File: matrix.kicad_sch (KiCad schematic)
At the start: 134 parts, among them SW1 ESC`, SW10 #9, SW11 #0, SW12 -_, SW13 =+, SW14 BACKSPACE, SW15 DELETE, SW16 TAB, SW17 Q, SW18 W, SW19 E, SW2 #1, SW20 R, SW21 T, SW22 Y, SW23 U, SW24 I, SW25 O, SW26 P, SW27 [{, SW28 }], SW29 \|, SW3 #2, SW30 PAGEDN, SW31 CAPSLOCK, SW32 A, SW33 S, SW34 D, SW35 F, SW36 G, SW37 H, SW38 J, SW39 K, SW4 #3, SW40 L, SW41 ;:, SW42 '", SW43 ENTER, SW44 INSERT, SW45 SHIFT, SW46 Z, SW47 X, SW48 C, SW49 V, SW5 #4, SW50 B, SW51 N, SW52 M, SW53 ,<, SW54 .>, SW55 /?, SW56 CAPSLOCK, SW57 UP, SW58 SHIFT, SW59 CTRL, SW6 #5, SW60 ALT, SW61 COMMAND, SW62 SPACE, SW63 ALT, SW64 `~, SW65 LEFT, SW66 DOWN, SW67 RIGHT, SW7 #6, SW8 #7, SW9 #8

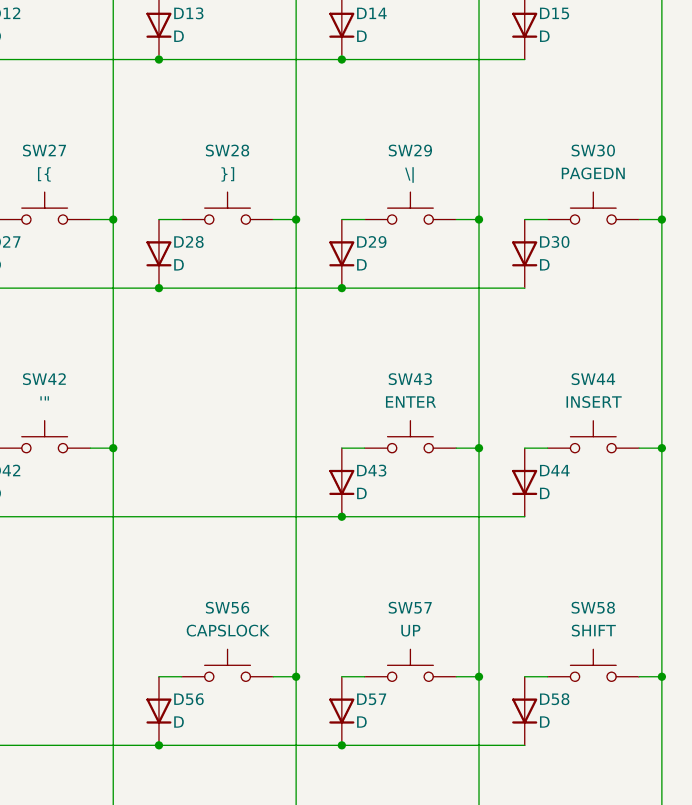
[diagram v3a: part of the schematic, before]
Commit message: PCB Started
need to properly locate pcb components
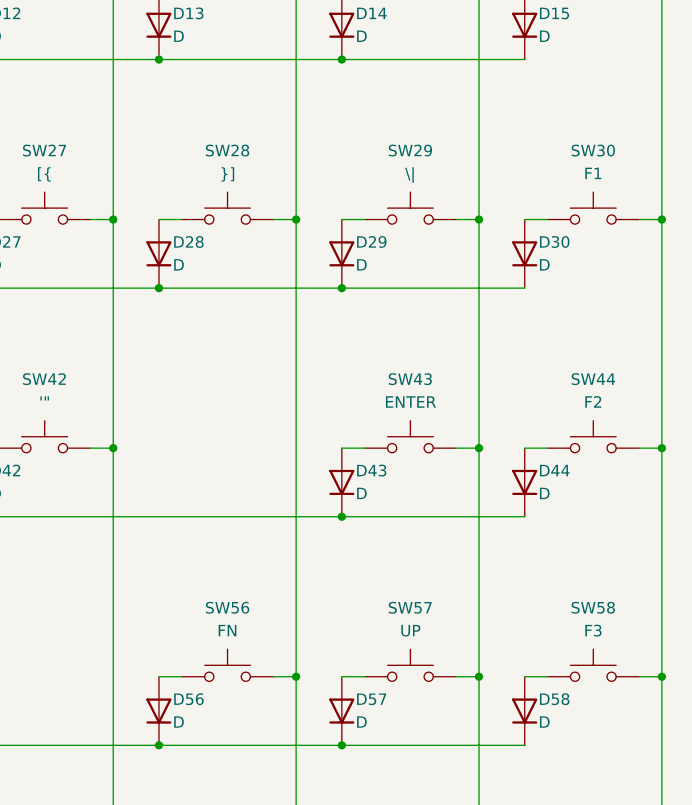
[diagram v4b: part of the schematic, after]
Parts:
- SW14: footprint Alps_Only:ALPS-1U -> Alps_Only:ALPS-2U
- SW16, SW29, SW59, SW61: footprint Alps_Only:ALPS-1U -> Alps_Only:ALPS-1.5U
- SW30: value PAGEDN -> F1
- SW31: footprint Alps_Only:ALPS-1U -> Alps_Only:ALPS-1.75U
- SW43, SW45: footprint Alps_Only:ALPS-1U -> Alps_Only:ALPS-2.25U
- SW44: value INSERT -> F2
- SW56: value CAPSLOCK -> FN; footprint Alps_Only:ALPS-1U -> Alps_Only:ALPS-1.75U
- SW58: value SHIFT -> F3
- SW60, SW63: footprint Alps_Only:ALPS-1U -> Alps_Only:ALPS-1.25U
- SW62: footprint Alps_Only:ALPS-1U -> Alps_Only:ALPS-6.5U
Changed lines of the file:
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@@
 			)
 		)
-		(property "Value" "PAGEDN"
+		(property "Value" "F1"
 			(at 341.63 67.31 0)
 			(effects
@@
 			)
 		)
-		(property "Value" "INSERT"
+		(property "Value" "F2"
 			(at 341.63 92.71 0)
 			(effects
@@
 			)
 		)
-		(property "Value" "SHIFT"
+		(property "Value" "F3"
 			(at 341.63 118.11 0)
 			(effects
@@
 			)
 		)
-		(property "Footprint" "Alps_Only:ALPS-1U"
+		(property "Footprint" "Alps_Only:ALPS-1.5U"
 			(at 321.31 67.31 0)
 			(effects
@@
 			)
 		)
-		(property "Footprint" "Alps_Only:ALPS-1U"
+		(property "Footprint" "Alps_Only:ALPS-2.25U"
 			(at 57.15 118.11 0)
 			(effects
@@
 			)
 		)
-		(property "Footprint" "Alps_Only:ALPS-1U"
+		(property "Footprint" "Alps_Only:ALPS-1.75U"
 			(at 57.15 92.71 0)
 			(effects
@@
 			)
 		)
-		(property "Footprint" "Alps_Only:ALPS-1U"
+		(property "Footprint" "Alps_Only:ALPS-1.5U"
 			(at 97.79 143.51 0)
 			(effects
@@
 			)
 		)
-		(property "Footprint" "Alps_Only:ALPS-1U"
+		(property "Footprint" "Alps_Only:ALPS-1.25U"
 			(at 260.35 143.51 0)
 			(effects
@@
 			)
 		)
-		(property "Footprint" "Alps_Only:ALPS-1U"
+		(property "Footprint" "Alps_Only:ALPS-2.25U"
 			(at 321.31 92.71 0)
 			(effects
@@
 			)
 		)
-		(property "Footprint" "Alps_Only:ALPS-1U"
+		(property "Footprint" "Alps_Only:ALPS-1.5U"
 			(at 57.15 67.31 0)
 			(effects
@@
 			)
 		)
-		(property "Value" "CAPSLOCK"
+		(property "Value" "FN"
 			(at 300.99 118.11 0)
 			(effects
@@
 			)
 		)
-		(property "Footprint" "Alps_Only:ALPS-1U"
+		(property "Footprint" "Alps_Only:ALPS-1.75U"
 			(at 300.99 118.11 0)
 			(effects
@@
 			)
 		)
-		(property "Footprint" "Alps_Only:ALPS-1U"
+		(property "Footprint" "Alps_Only:ALPS-2U"
 			(at 321.31 41.91 0)
 			(effects
@@
 			)
 		)
-		(property "Footprint" "Alps_Only:ALPS-1U"
+		(property "Footprint" "Alps_Only:ALPS-1.5U"
 			(at 57.15 143.51 0)
 			(effects
@@
 			)
 		)
-		(property "Footprint" "Alps_Only:ALPS-1U"
+		(property "Footprint" "Alps_Only:ALPS-6.5U"
 			(at 179.07 143.51 0)
 			(effects
@@
 			)
 		)
-		(property "Footprint" "Alps_Only:ALPS-1U"
+		(property "Footprint" "Alps_Only:ALPS-1.25U"
 			(at 77.47 143.51 0)
 			(effects

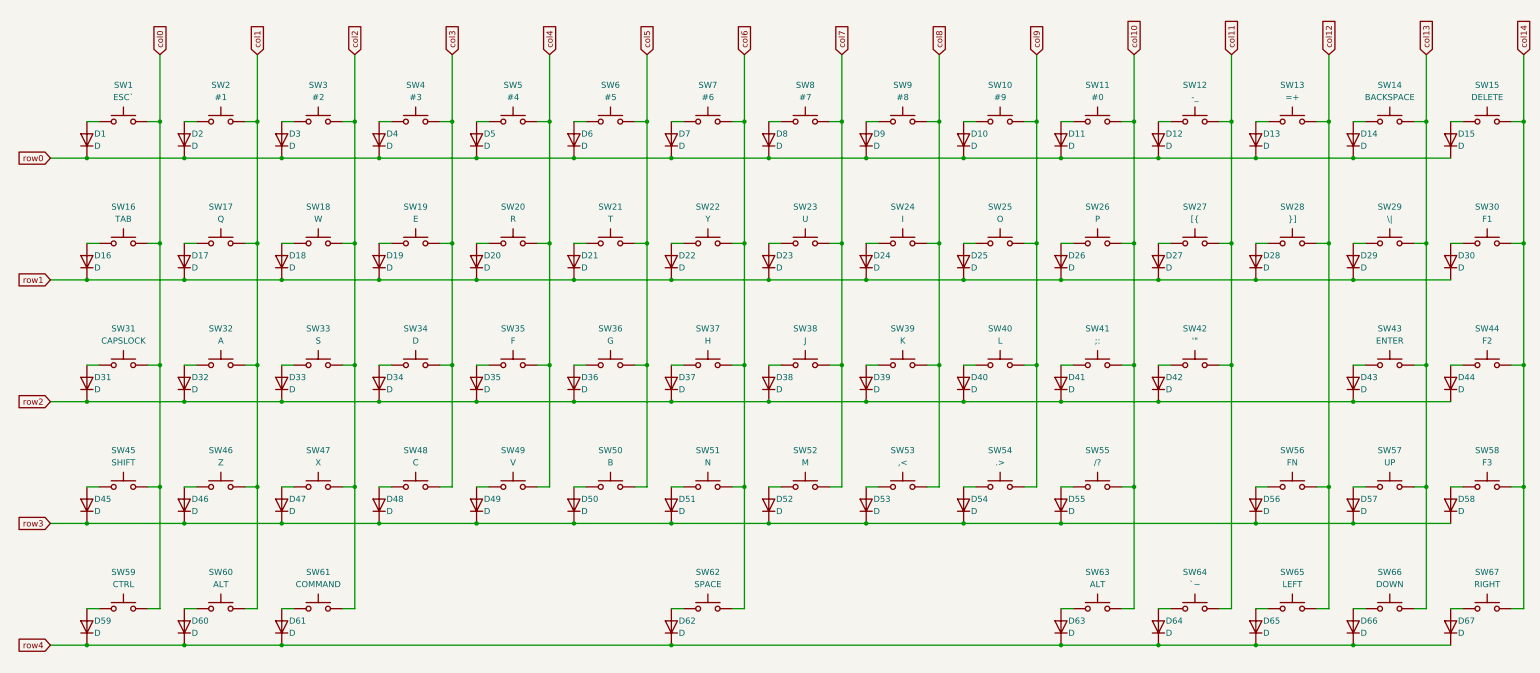
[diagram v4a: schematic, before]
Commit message: Switch (SW_PUSH) Orientation Flip
rotated SW_PUSH in schematic to align with tutorial
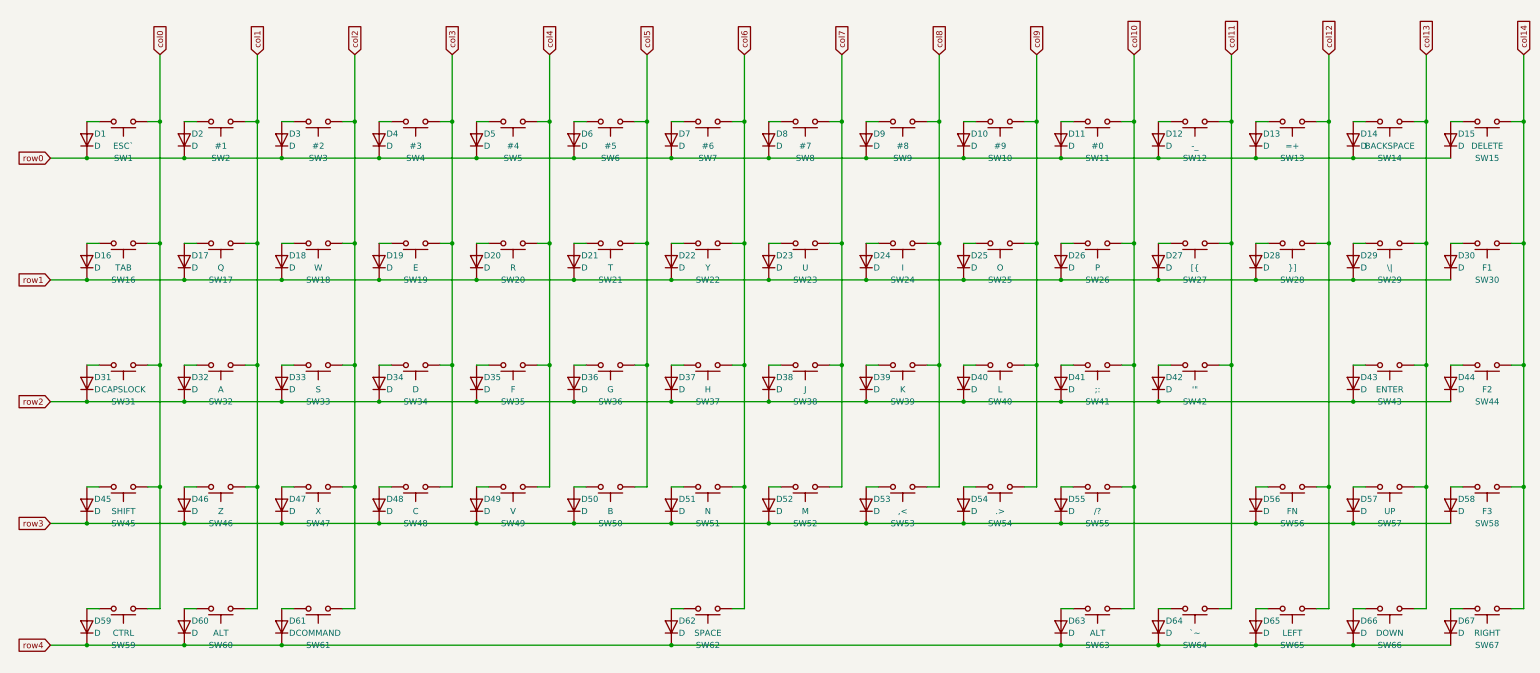
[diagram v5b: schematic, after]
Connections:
- net col0: now also SW1.1, SW16.1, SW31.1, SW45.1, SW59.1; no longer SW1.2, SW16.2, SW31.2, SW45.2, SW59.2
- net col1: now also SW17.1, SW2.1, SW32.1, SW46.1, SW60.1; no longer SW17.2, SW2.2, SW32.2, SW46.2, SW60.2
- net col10: now also SW11.1, SW26.1, SW41.1, SW55.1, SW63.1; no longer SW11.2, SW26.2, SW41.2, SW55.2, SW63.2
- net col11: now also SW12.1, SW27.1, SW42.1, SW64.1; no longer SW12.2, SW27.2, SW42.2, SW64.2
- net col12: now also SW13.1, SW28.1, SW56.1, SW65.1; no longer SW13.2, SW28.2, SW56.2, SW65.2
- net col13: now also SW14.1, SW29.1, SW43.1, SW57.1, SW66.1; no longer SW14.2, SW29.2, SW43.2, SW57.2, SW66.2
- net col14: now also SW15.1, SW30.1, SW44.1, SW58.1, SW67.1; no longer SW15.2, SW30.2, SW44.2, SW58.2, SW67.2
- net col2: now also SW18.1, SW3.1, SW33.1, SW47.1, SW61.1; no longer SW18.2, SW3.2, SW33.2, SW47.2, SW61.2
- net col3: now also SW19.1, SW34.1, SW4.1, SW48.1; no longer SW19.2, SW34.2, SW4.2, SW48.2
- net col4: now also SW20.1, SW35.1, SW49.1, SW5.1; no longer SW20.2, SW35.2, SW49.2, SW5.2
- net col5: now also SW21.1, SW36.1, SW50.1, SW6.1; no longer SW21.2, SW36.2, SW50.2, SW6.2
- net col6: now also SW22.1, SW37.1, SW51.1, SW62.1, SW7.1; no longer SW22.2, SW37.2, SW51.2, SW62.2, SW7.2
- net col7: now also SW23.1, SW38.1, SW52.1, SW8.1; no longer SW23.2, SW38.2, SW52.2, SW8.2
- net col8: now also SW24.1, SW39.1, SW53.1, SW9.1; no longer SW24.2, SW39.2, SW53.2, SW9.2
- net col9: now also SW10.1, SW25.1, SW40.1, SW54.1; no longer SW10.2, SW25.2, SW40.2, SW54.2
- net at D20.2 (A): now also SW20.2; no longer SW20.1
- net at D30.2 (A): now also SW30.2; no longer SW30.1
- net at D41.2 (A): now also SW41.2; no longer SW41.1
- net at D50.2 (A): now also SW50.2; no longer SW50.1
- net at D19.2 (A): now also SW19.2; no longer SW19.1
- net at D65.2 (A): now also SW65.2; no longer SW65.1
- net at D46.2 (A): now also SW46.2; no longer SW46.1
- net at D13.2 (A): now also SW13.2; no longer SW13.1
- net at D31.2 (A): now also SW31.2; no longer SW31.1
- net at D67.2 (A): now also SW67.2; no longer SW67.1
- net at D27.2 (A): now also SW27.2; no longer SW27.1
- net at D24.2 (A): now also SW24.2; no longer SW24.1
- net at D44.2 (A): now also SW44.2; no longer SW44.1
- net at D11.2 (A): now also SW11.2; no longer SW11.1
- net at D58.2 (A): now also SW58.2; no longer SW58.1
- net at D4.2 (A): now also SW4.2; no longer SW4.1
- net at D64.2 (A): now also SW64.2; no longer SW64.1
- net at D66.2 (A): now also SW66.2; no longer SW66.1
- net at D7.2 (A): now also SW7.2; no longer SW7.1
- net at D33.2 (A): now also SW33.2; no longer SW33.1
- net at D49.2 (A): now also SW49.2; no longer SW49.1
- net at D15.2 (A): now also SW15.2; no longer SW15.1
- net at D29.2 (A): now also SW29.2; no longer SW29.1
- net at D1.2 (A): now also SW1.2; no longer SW1.1
- net at D28.2 (A): now also SW28.2; no longer SW28.1
- net at D45.2 (A): now also SW45.2; no longer SW45.1
- net at D32.2 (A): now also SW32.2; no longer SW32.1
- net at D53.2 (A): now also SW53.2; no longer SW53.1
- net at D38.2 (A): now also SW38.2; no longer SW38.1
- net at D61.2 (A): now also SW61.2; no longer SW61.1
- net at D63.2 (A): now also SW63.2; no longer SW63.1
- net at D5.2 (A): now also SW5.2; no longer SW5.1
- net at D21.2 (A): now also SW21.2; no longer SW21.1
- net at D18.2 (A): now also SW18.2; no longer SW18.1
- net at D23.2 (A): now also SW23.2; no longer SW23.1
- net at D34.2 (A): now also SW34.2; no longer SW34.1
- net at D52.2 (A): now also SW52.2; no longer SW52.1
- net at D54.2 (A): now also SW54.2; no longer SW54.1
- net at D55.2 (A): now also SW55.2; no longer SW55.1
- net at D22.2 (A): now also SW22.2; no longer SW22.1
- net at D40.2 (A): now also SW40.2; no longer SW40.1
- net at D17.2 (A): now also SW17.2; no longer SW17.1
- net at D43.2 (A): now also SW43.2; no longer SW43.1
- net at D6.2 (A): now also SW6.2; no longer SW6.1
- net at D51.2 (A): now also SW51.2; no longer SW51.1
- net at D16.2 (A): now also SW16.2; no longer SW16.1
- net at D36.2 (A): now also SW36.2; no longer SW36.1
- net at D2.2 (A): now also SW2.2; no longer SW2.1
- net at D9.2 (A): now also SW9.2; no longer SW9.1
- net at D47.2 (A): now also SW47.2; no longer SW47.1
- net at D57.2 (A): now also SW57.2; no longer SW57.1
- net at D48.2 (A): now also SW48.2; no longer SW48.1
- net at D42.2 (A): now also SW42.2; no longer SW42.1
- net at D35.2 (A): now also SW35.2; no longer SW35.1
- net at D26.2 (A): now also SW26.2; no longer SW26.1
- net at D39.2 (A): now also SW39.2; no longer SW39.1
- net at D3.2 (A): now also SW3.2; no longer SW3.1
- net at D8.2 (A): now also SW8.2; no longer SW8.1
- net at D59.2 (A): now also SW59.2; no longer SW59.1
- net at D12.2 (A): now also SW12.2; no longer SW12.1
- net at D56.2 (A): now also SW56.2; no longer SW56.1
- net at D37.2 (A): now also SW37.2; no longer SW37.1
- net at D14.2 (A): now also SW14.2; no longer SW14.1
- net at D10.2 (A): now also SW10.2; no longer SW10.1
- net at D25.2 (A): now also SW25.2; no longer SW25.1
- net at D60.2 (A): now also SW60.2; no longer SW60.1
- net at D62.2 (A): now also SW62.2; no longer SW62.1
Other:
- moved on the sheet: SW1, SW10, SW11, SW12, SW13, SW14, SW15, SW16, SW17, SW18, SW19, SW2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
